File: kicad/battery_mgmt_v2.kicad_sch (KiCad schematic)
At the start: 18 parts, among them J301 BATTERY_CONN, Q302 2N7002, U303 BQ25185, U304 TPS7A20

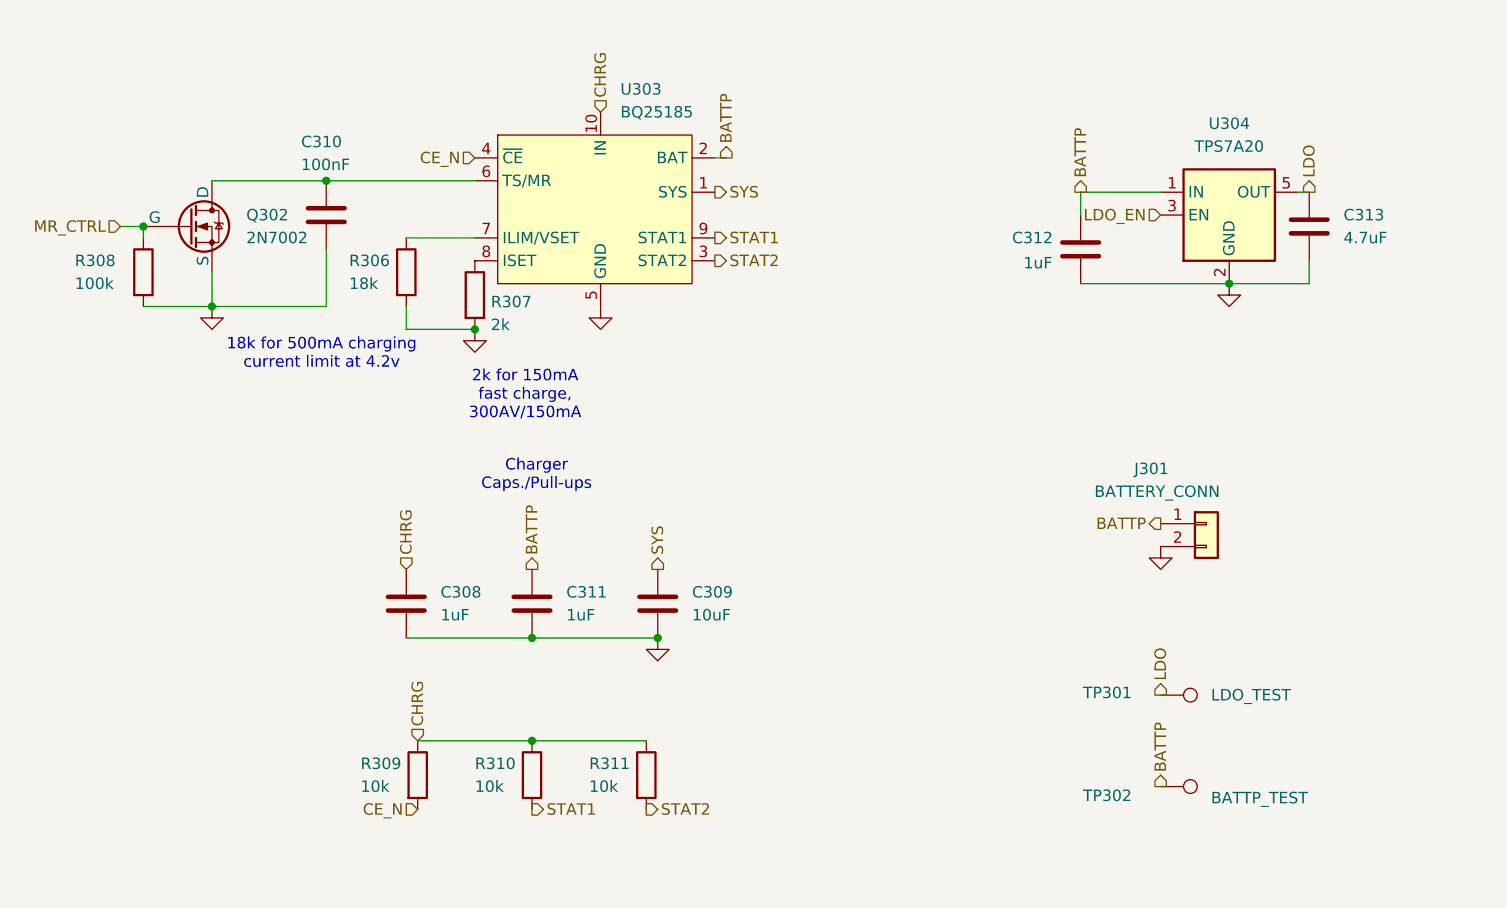
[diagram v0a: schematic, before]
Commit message: slight refactoring, fix LDO power-path
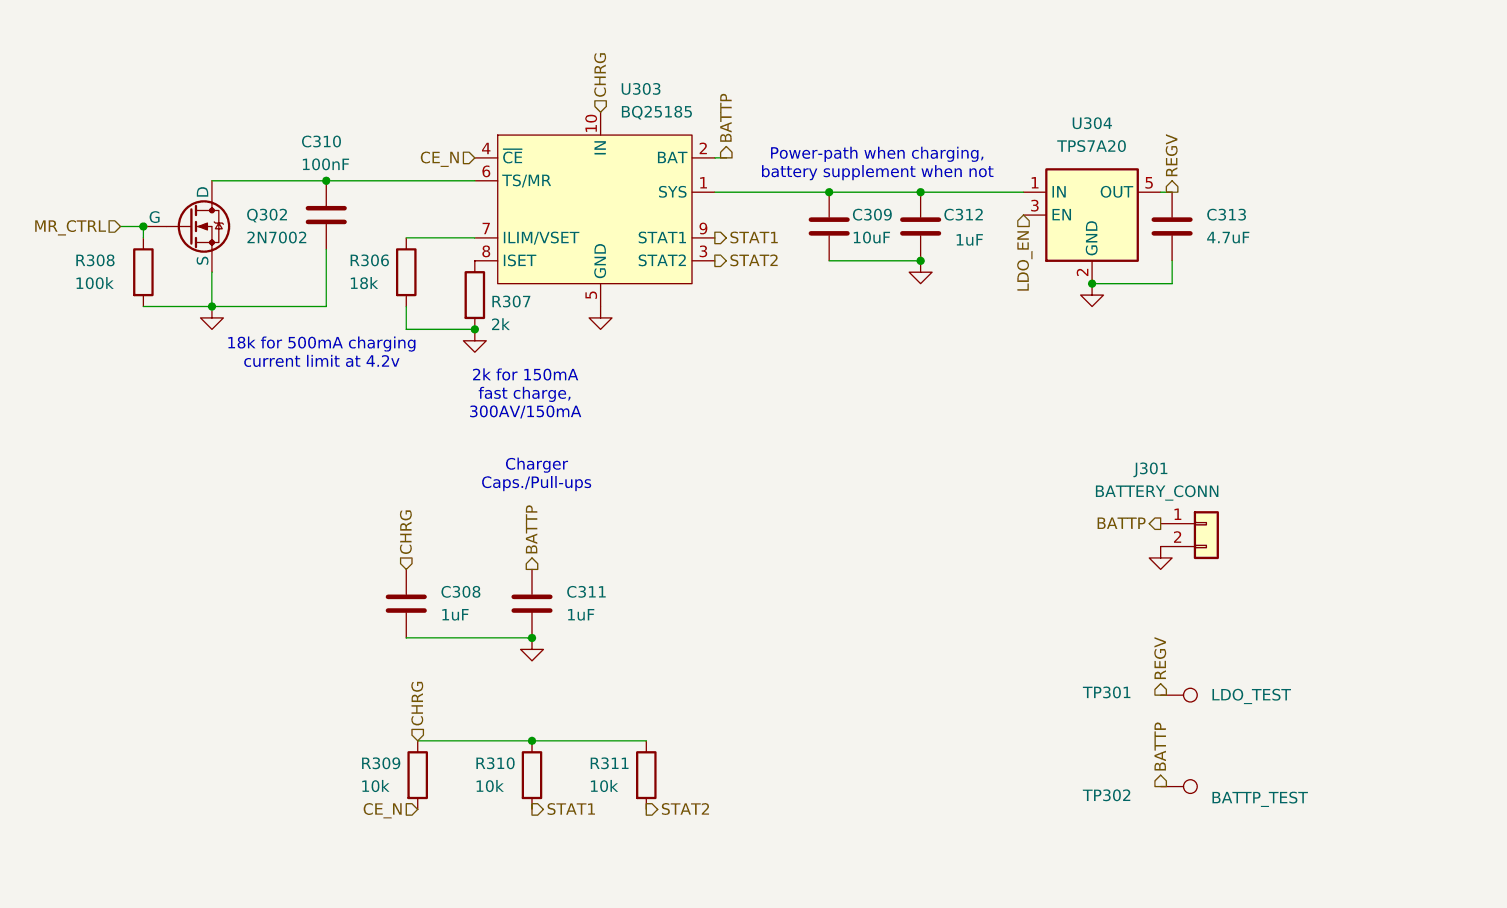
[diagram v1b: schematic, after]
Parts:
- U303: footprint (none) -> Raven:WSON10_DLH_TEX-M
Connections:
- net BATTP: no longer C312.1, U304.1 (IN)
- net LDO renamed REGV
- net SYS: no longer names the net of C309.1, U303.1 (SYS)
- net SYS: now also C312.1, U304.1 (IN)
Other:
- note added: "Power-path when charging, battery supplement when not"
- moved on the sheet: C309, C312, C313, U304

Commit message: finish management schematic, ready for PCB
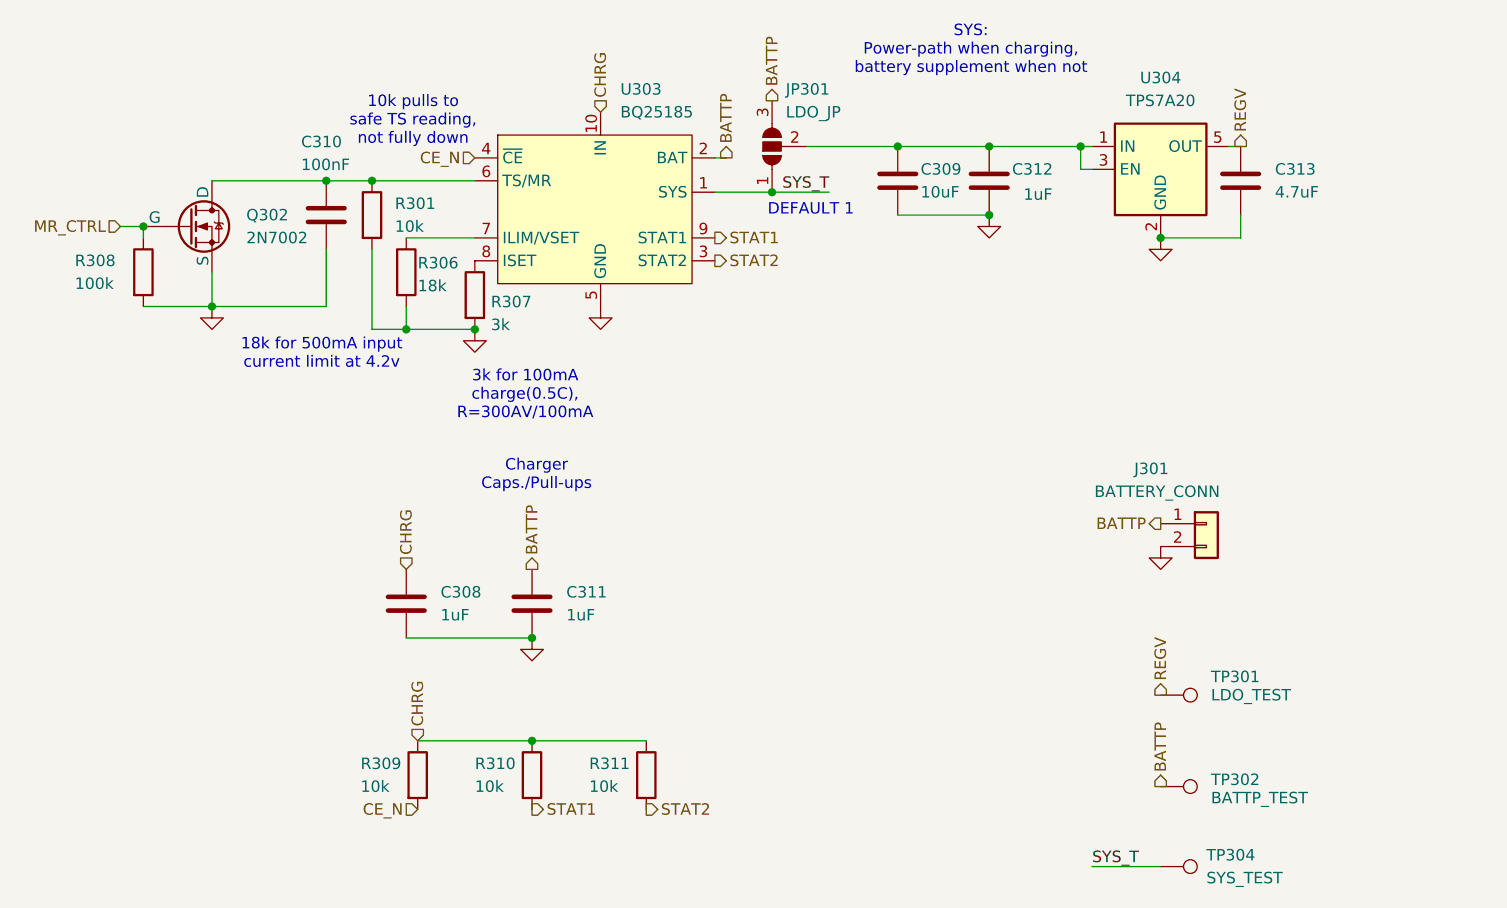
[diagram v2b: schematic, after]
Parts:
- added JP301: LDO_JP, Jumper:SolderJumper-3_P2.0mm_Open_TrianglePad1.0x1.5mm_NumberLabels, symbol Jumper:SolderJumper_3_Open
- added R301: 10k, Resistor_SMD:R_0603_1608Metric_Pad0.98x0.95mm_HandSolder, symbol Device:R
- added TP304: SYS_TEST, TestPoint:TestPoint_Pad_D1.5mm, symbol Connector:TestPoint
- C308, C311, C312, C313: footprint (none) -> Capacitor_SMD:C_0805_2012Metric_Pad1.18x1.45mm_HandSolder
- C309: footprint (none) -> Capacitor_SMD:C_0603_1608Metric_Pad1.08x0.95mm_HandSolder
- R306, R309, R310, R311: footprint (none) -> Resistor_SMD:R_0603_1608Metric_Pad0.98x0.95mm_HandSolder
- R307: value 2k -> 3k; footprint (none) -> Resistor_SMD:R_0603_1608Metric_Pad0.98x0.95mm_HandSolder
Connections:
- net LDO_EN is gone; now on an unnamed net: U304.3 (EN)
- net BATTP: now also JP301.3 (B)
- net GND: now also R301.2
- net at C310.1, Q302.1 (D), U303.6 (TS/MR): now also R301.1
- net at C309.1, C312.1, U304.1 (IN): now also JP301.2 (C); no longer U303.1 (SYS)
- new net SYS_T: JP301.1 (A), TP304.1, U303.1 (SYS)
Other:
- note added: "10k pulls to safe TS reading, not fully down"
- note added: "18k for 500mA input current limit at 4.2v"
- note added: "3k for 100mA charge(0.5C), R=300AV/100mA"
- note added: "DEFAULT 1"
- note added: "SYS: Power-path when charging, battery supplement when not"
- note removed: "18k for 500mA charging current limit at 4.2v"
- note removed: "2k for 150mA fast charge, 300AV/150mA"
- note removed: "Power-path when charging, battery supplement when not"
- moved on the sheet: C309, C312, C313, U304

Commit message: finish battery PCB layout, PCB refactoring
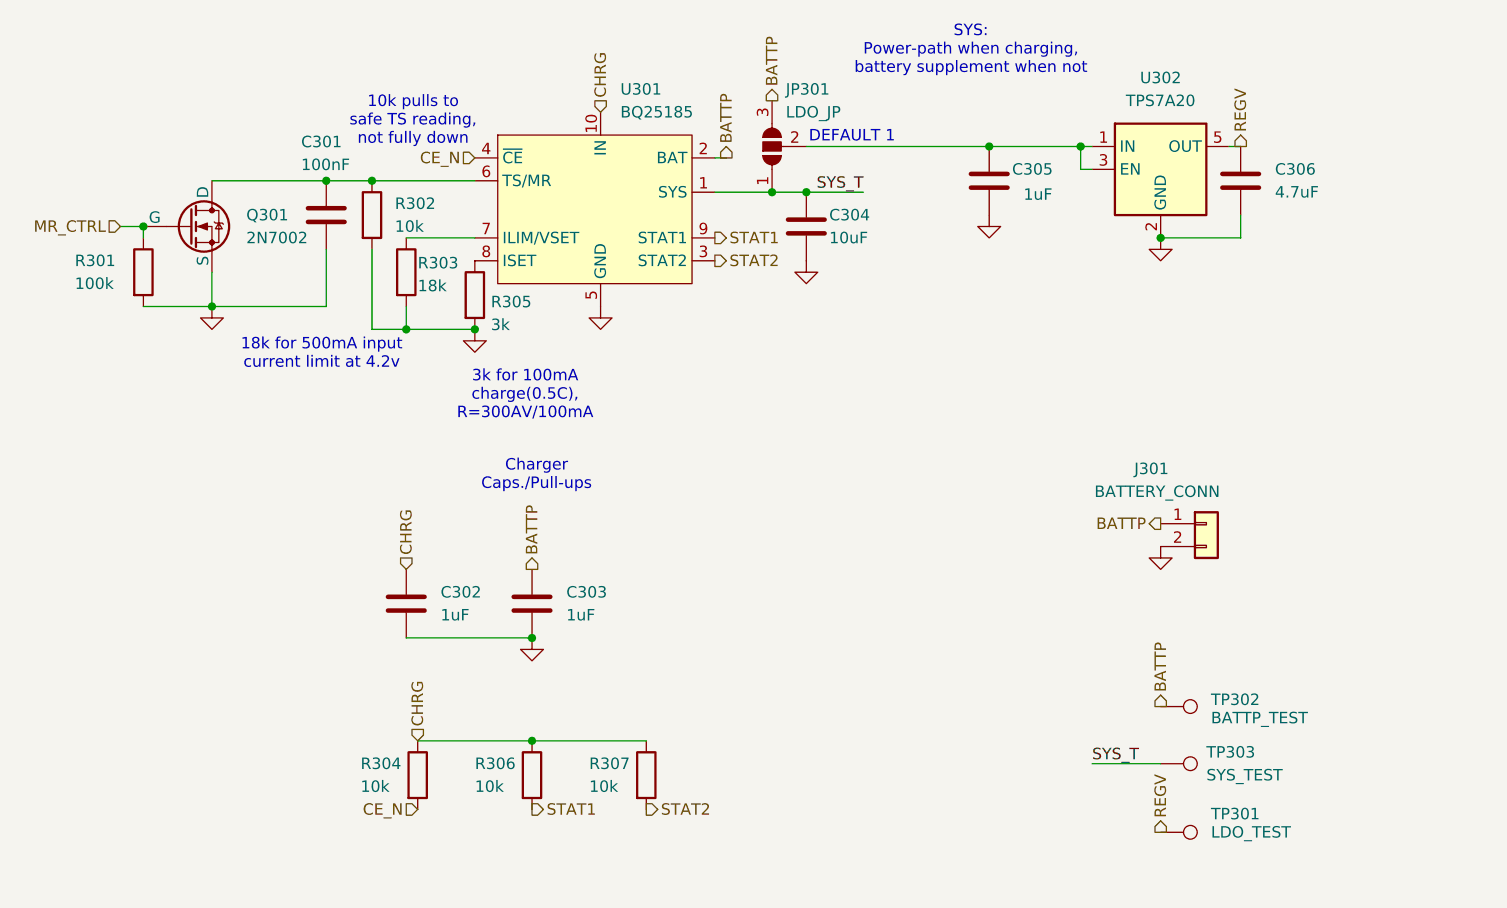
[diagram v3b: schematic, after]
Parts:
- renumbered C310 to C301, C308 to C302, C311 to C303, C309 to C304, C312 to C305, C313 to C306, Q302 to Q301, R308 to R301, R301 to R302, R306 to R303, R309 to R304, R307 to R305, R310 to R306, R311 to R307, TP304 to TP303, U303 to U301, U304 to U302
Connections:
- net GND: now also U301.11 (NC), U302.4 (NC)
- net SYS_T: now also C304.1
- net at C305.1, JP301.2 (C), U302.1 (IN)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: no longer C304.1
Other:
- moved on the sheet: C304, TP301, TP302, TP303

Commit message: Revision 2: Fix MOSFET pins and various changes
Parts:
- renumbered TP302 to TP301, TP303 to TP302, TP301 to TP303
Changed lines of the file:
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@@
 		(dnp no)
 		(fields_autoplaced yes)
-		(property "Reference" "#PWR0305"
+		(property "Reference" "#PWR0306"
 			(at 171.45 80.01 0)
 			(effects
@@
 			(project "kicad"
 				(path "/97e37379-fec6-4f0d-82d9-4ea53516bb02/d2226d13-9ee7-410c-817d-a66f223af34c"
-					(reference "#PWR0305")
+					(reference "#PWR0306")
 					(unit 1)
 				)
@@
 		(on_board yes)
 		(dnp no)
-		(property "Reference" "TP302"
+		(property "Reference" "TP301"
 			(at 196.088 127.508 90)
 			(effects
@@
 			(project "kicad"
 				(path "/97e37379-fec6-4f0d-82d9-4ea53516bb02/d2226d13-9ee7-410c-817d-a66f223af34c"
-					(reference "TP302")
+					(reference "TP301")
 					(unit 1)
 				)
@@
 		(dnp no)
 		(fields_autoplaced yes)
-		(property "Reference" "#PWR0306"
+		(property "Reference" "#PWR0307"
 			(at 190.5 82.55 0)
 			(effects
@@
 			(project "kicad"
 				(path "/97e37379-fec6-4f0d-82d9-4ea53516bb02/d2226d13-9ee7-410c-817d-a66f223af34c"
-					(reference "#PWR0306")
+					(reference "#PWR0307")
 					(unit 1)
 				)
@@
 		(on_board yes)
 		(dnp no)
-		(property "Reference" "TP301"
+		(property "Reference" "TP303"
 			(at 196.088 140.208 90)
 			(effects
@@
 			(project "kicad"
 				(path "/97e37379-fec6-4f0d-82d9-4ea53516bb02/d2226d13-9ee7-410c-817d-a66f223af34c"
-					(reference "TP301")
+					(reference "TP303")
 					(unit 1)
 				)
@@
 		(dnp no)
 		(fields_autoplaced yes)
-		(property "Reference" "TP303"
+		(property "Reference" "TP302"
 			(at 195.58 133.3499 90)
 			(effects
@@
 			(project "kicad"
 				(path "/97e37379-fec6-4f0d-82d9-4ea53516bb02/d2226d13-9ee7-410c-817d-a66f223af34c"
-					(reference "TP303")
+					(reference "TP302")
 					(unit 1)
 				)
@@
 		(dnp no)
 		(fields_autoplaced yes)
-		(property "Reference" "#PWR0307"
+		(property "Reference" "#PWR0308"
 			(at 190.5 116.84 0)
 			(effects
@@
 			(project "kicad"
 				(path "/97e37379-fec6-4f0d-82d9-4ea53516bb02/d2226d13-9ee7-410c-817d-a66f223af34c"
-					(reference "#PWR0307")
+					(reference "#PWR0308")
 					(unit 1)
 				)
@@
 		(dnp no)
 		(fields_autoplaced yes)
-		(property "Reference" "#PWR0308"
+		(property "Reference" "#PWR0305"
 			(at 151.13 85.09 0)
 			(effects
@@
 			(project "kicad"
 				(path "/97e37379-fec6-4f0d-82d9-4ea53516bb02/d2226d13-9ee7-410c-817d-a66f223af34c"
-					(reference "#PWR0308")
-					(unit 1)
-				)
+					(reference "#PWR0305")
+					(unit 1)
+				)

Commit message: Unfinished switch additions and fixes
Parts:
- removed JP301: LDO_JP, Jumper:SolderJumper-3_P2.0mm_Open_TrianglePad1.0x1.5mm_NumberLabels, symbol Jumper:SolderJumper_3_Open
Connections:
- net SYS_T: now also C305.1, U302.1 (IN), U302.3 (EN)
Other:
- note added: "Power switch handled outside the module"
- note removed: "DEFAULT 1"
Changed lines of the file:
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@@
+	)
+	(junction
+		(at 146.05 71.12)
+		(diameter 0)
+		(color 0 0 0 0)
 	)
 	(junction
@@
 	)
 	(junction
-		(at 147.32 71.12)
-		(diameter 0)
-		(color 0 0 0 0)
-	)
-	(junction
 		(at 171.45 66.04)
 		(diameter 0)
@@
 	(wire
 		(pts
+			(xy 146.05 71.12) (xy 151.13 71.12)
+		)
+		(stroke
+			(width 0)
+			(type default)
+		)
+	)
+	(wire
+		(pts
 			(xy 190.5 134.62) (xy 182.88 134.62)
 		)
@@
 	(wire
 		(pts
+			(xy 146.05 66.04) (xy 146.05 71.12)
+		)
+		(stroke
+			(width 0)
+			(type default)
+		)
+	)
+	(wire
+		(pts
 			(xy 97.79 77.47) (xy 97.79 83.82)
 		)
@@
 	(wire
 		(pts
-			(xy 140.97 71.12) (xy 147.32 71.12)
-		)
-		(stroke
-			(width 0)
-			(type default)
-		)
-	)
-	(wire
-		(pts
 			(xy 142.24 67.31) (xy 140.97 67.31)
 		)
@@
 	(wire
 		(pts
-			(xy 147.32 71.12) (xy 151.13 71.12)
+			(xy 140.97 71.12) (xy 146.05 71.12)
 		)
 		(stroke
@@
 	(wire
 		(pts
+			(xy 146.05 66.04) (xy 171.45 66.04)
+		)
+		(stroke
+			(width 0)
+			(type default)
+		)
+	)
+	(wire
+		(pts
 			(xy 97.79 69.85) (xy 102.87 69.85)
 		)
@@
 		)
 	)
-	(wire
-		(pts
-			(xy 151.13 66.04) (xy 171.45 66.04)
-		)
-		(stroke
-			(width 0)
-			(type default)
-		)
-	)
 	(text "SYS:\nPower-path when charging,\nbattery supplement when not"
 		(exclude_from_sim no)
@@
 		)
 	)
+	(text "Power switch handled\noutside the module"
+		(exclude_from_sim no)
+		(at 214.376 61.976 0)
+		(effects
+			(font
+				(size 1.27 1.27)
+			)
+		)
+	)
 	(text "10k pulls to\nsafe TS reading,\nnot fully down"
 		(exclude_from_sim no)
@@
 		(exclude_from_sim no)
 		(at 97.282 89.154 0)
-		(effects
-			(font
-				(size 1.27 1.27)
-			)
-		)
-	)
-	(text "DEFAULT 1"
-		(exclude_from_sim no)
-		(at 156.21 65.024 0)
 		(effects
 			(font
@@
 			)
 			(justify right)
-		)
-	)
-	(hierarchical_label "BATTP"
-		(shape output)
-		(at 147.32 60.96 90)
-		(fields_autoplaced yes)
-		(effects
-			(font
-				(size 1.27 1.27)
-			)
-			(justify left)
 		)
 	)
@@
 					(unit 1)
 				)
-			)
-		)
-	)
-	(symbol
-		(lib_id "Jumper:SolderJumper_3_Open")
-		(at 147.32 66.04 90)
-		(unit 1)
-		(exclude_from_sim yes)
-		(in_bom no)
-		(on_board yes)
-		(dnp no)
-		(property "Reference" "JP301"
-			(at 148.844 59.69 90)
-			(effects
-				(font
-					(size 1.27 1.27)
-				)
-				(justify right)
-			)
-		)
-		(property "Value" "LDO_JP"
-			(at 148.844 62.23 90)
-			(effects
-				(font
-					(size 1.27 1.27)
-				)
-				(justify right)
-			)
-		)
-		(property "Footprint" "Jumper:SolderJumper-3_P2.0mm_Open_TrianglePad1.0x1.5mm_NumberLabels"
-			(at 147.32 66.04 0)
-			(effects
-				(font
-					(size 1.27 1.27)
-				)
-				(hide yes)
-			)
-		)
-		(property "Datasheet" "~"
-			(at 147.32 66.04 0)
-			(effects
-				(font
-					(size 1.27 1.27)
-				)
-				(hide yes)
-			)
-		)
-		(property "Description" "Solder Jumper, 3-pole, open"
-			(at 147.32 66.04 0)
-			(effects
-				(font
-					(size 1.27 1.27)
-				)
-				(hide yes)
-			)
-		)
-		(pin "2"
-		)
-		(pin "1"
-		)
-		(pin "3"
-		)
-		(instances
-			(project "kicad"
-				(path "/97e37379-fec6-4f0d-82d9-4ea53516bb02/d2226d13-9ee7-410c-817d-a66f223af34c"
-					(reference "JP301")
-					(unit 1)
-				)

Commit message: Part updates
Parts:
- TP301, TP302, TP303: footprint TestPoint:TestPoint_Pad_D1.5mm -> TestPoint:TestPoint_Pad_D1.0mm
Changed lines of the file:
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@@
 			)
 		)
-		(property "Footprint" "TestPoint:TestPoint_Pad_D1.5mm"
+		(property "Footprint" "TestPoint:TestPoint_Pad_D1.0mm"
 			(at 190.5 133.35 0)
 			(effects
@@
 			)
 		)
-		(property "Footprint" "TestPoint:TestPoint_Pad_D1.5mm"
+		(property "Footprint" "TestPoint:TestPoint_Pad_D1.0mm"
 			(at 190.5 147.32 0)
 			(effects
@@
 			)
 		)
-		(property "Footprint" "TestPoint:TestPoint_Pad_D1.5mm"
+		(property "Footprint" "TestPoint:TestPoint_Pad_D1.0mm"
 			(at 190.5 139.7 0)
 			(effects
